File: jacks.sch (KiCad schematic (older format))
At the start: 72 parts, among them J1 PJ301CM, J10 PJ301BM, J11 PJ301BM, J12 PJ301BM, J13 PJ301BM, J14 PJ301BM, J15 PJ301BM, J16 PJ301BM, J17 PJ301BM, J18 PJ301BM, J19 PJ301BM, J2 PJ301CM, J20 PJ301BM, J21 PJ301BM, J22 PJ301BM, J23 PJ301BM, J24 PJ301BM, J25 PJ301BM, J26 PJ301BM, J3 PJ301BM, J4 PJ301BM, J5 PJ301BM, J6 PJ301BM, J7 PJ301BM, J8 PJ301BM, J9 PJ301BM, Q1 MMBT3904, Q2 MMBT3904, Q3 MMBT3904, Q4 MMBT3904, U1 VO0600T, U2 74LV1T34, U6 TL074

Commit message: added package field
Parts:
- C10, C11, C22, C23, C7, C8, R1, R12, R13, R14, R15, R16, R17, R18, R19, R2, R24, R25, R28, R29, R3, R30, R31, R35, R36, R37, R38, R4, R43, R44, R66, R76, R78, R79, R81, R82, R83, R84: Package (none) -> 0603
- D2: Package (none) -> SOD-123
- Q1, Q2, Q3, Q4: Package (none) -> SOT-23
- U1: Package (none) -> SOIC-8
- U2: Package (none) -> SOT-23-5
- U6: Package (none) -> SOIC-14
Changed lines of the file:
@@
 F 4 "ON Semiconductor" H 2100 1875 50  0001 C CNN "MFN"
 F 5 "MMBT3904LT1G" H 2100 1875 50  0001 C CNN "MFP"
+F 6 "SOT-23" H 2100 1875 50  0001 C CNN "Package"
 	1    1900 1700
 	1    0    0    -1
@@
 F 4 "Panasonic" H 1530 1800 50  0001 C CNN "MFN"
 F 5 "ERJ-3EKF1003V" H 1530 1800 50  0001 C CNN "MFP"
+F 6 "0603" H 1530 1800 50  0001 C CNN "Package"
 	1    1450 1700
 	0    1    1    0
@@
 F 4 "Panasonic" H 2080 1250 50  0001 C CNN "MFN"
 F 5 "ERJ-3EKF1002V" H 2080 1250 50  0001 C CNN "MFP"
+F 6 "0603" H 2080 1250 50  0001 C CNN "Package"
 	1    2000 1150
 	1    0    0    -1
@@
 F 4 "ON Semiconductor" H 2100 3475 50  0001 C CNN "MFN"
 F 5 "MMBT3904LT1G" H 2100 3475 50  0001 C CNN "MFP"
+F 6 "SOT-23" H 2100 3475 50  0001 C CNN "Package"
 	1    1900 3300
 	1    0    0    -1
@@
 F 4 "Panasonic" H 1530 3400 50  0001 C CNN "MFN"
 F 5 "ERJ-3EKF1003V" H 1530 3400 50  0001 C CNN "MFP"
+F 6 "0603" H 1530 3400 50  0001 C CNN "Package"
 	1    1450 3300
 	0    1    1    0
@@
 F 4 "Panasonic" H 2080 2850 50  0001 C CNN "MFN"
 F 5 "ERJ-3EKF1002V" H 2080 2850 50  0001 C CNN "MFP"
+F 6 "0603" H 2080 2850 50  0001 C CNN "Package"
 	1    2000 2750
 	1    0    0    -1
@@
 F 4 "ON Semiconductor" H 4100 1875 50  0001 C CNN "MFN"
 F 5 "MMBT3904LT1G" H 4100 1875 50  0001 C CNN "MFP"
+F 6 "SOT-23" H 4100 1875 50  0001 C CNN "Package"
 	1    3900 1700
 	1    0    0    -1
@@
 F 4 "Panasonic" H 4080 1250 50  0001 C CNN "MFN"
 F 5 "ERJ-3EKF1001V" H 4080 1250 50  0001 C CNN "MFP"
+F 6 "0603" H 4080 1250 50  0001 C CNN "Package"
 	1    4000 1150
 	1    0    0    -1
@@
 F 4 "Panasonic" H 3530 1800 50  0001 C CNN "MFN"
 F 5 "ERJ-3EKF1002V" H 3530 1800 50  0001 C CNN "MFP"
+F 6 "0603" H 3530 1800 50  0001 C CNN "Package"
 	1    3450 1700
 	0    1    1    0
@@
 F 4 "ON Semiconductor" H 4100 3575 50  0001 C CNN "MFN"
 F 5 "MMBT3904LT1G" H 4100 3575 50  0001 C CNN "MFP"
+F 6 "SOT-23" H 4100 3575 50  0001 C CNN "Package"
 	1    3900 3400
 	1    0    0    -1
@@
 F 4 "Panasonic" H 4080 2950 50  0001 C CNN "MFN"
 F 5 "ERJ-3EKF1001V" H 4080 2950 50  0001 C CNN "MFP"
+F 6 "0603" H 4080 2950 50  0001 C CNN "Package"
 	1    4000 2850
 	1    0    0    -1
@@
 F 4 "Panasonic" H 3530 3500 50  0001 C CNN "MFN"
 F 5 "ERJ-3EKF1002V" H 3530 3500 50  0001 C CNN "MFP"
+F 6 "0603" H 3530 3500 50  0001 C CNN "Package"
 	1    3450 3400
 	0    1    1    0
@@
 F 4 "Panasonic" H 10330 900 50  0001 C CNN "MFN"
 F 5 "ERJ-3EKF1001V" H 10330 900 50  0001 C CNN "MFP"
+F 6 "0603" H 10330 900 50  0001 C CNN "Package"
 	1    10250 800
 	0    1    1    0
@@
 F 4 "Panasonic" H 10330 1600 50  0001 C CNN "MFN"
 F 5 "ERJ-3EKF1001V" H 10330 1600 50  0001 C CNN "MFP"
+F 6 "0603" H 10330 1600 50  0001 C CNN "Package"
 	1    10250 1500
 	0    1    1    0
@@
 F 4 "Panasonic" H 10330 2300 50  0001 C CNN "MFN"
 F 5 "ERJ-3EKF1001V" H 10330 2300 50  0001 C CNN "MFP"
+F 6 "0603" H 10330 2300 50  0001 C CNN "Package"
 	1    10250 2200
 	0    1    1    0
@@
 F 4 "Panasonic" H 10330 3000 50  0001 C CNN "MFN"
 F 5 "ERJ-3EKF1001V" H 10330 3000 50  0001 C CNN "MFP"
+F 6 "0603" H 10330 3000 50  0001 C CNN "Package"
 	1    10250 2900
 	0    1    1    0
@@
 F 4 "Panasonic" H 10330 3700 50  0001 C CNN "MFN"
 F 5 "ERJ-3EKF1001V" H 10330 3700 50  0001 C CNN "MFP"
+F 6 "0603" H 10330 3700 50  0001 C CNN "Package"
 	1    10250 3600
 	0    1    1    0
@@
 F 4 "Panasonic" H 10330 4400 50  0001 C CNN "MFN"
 F 5 "ERJ-3EKF1001V" H 10330 4400 50  0001 C CNN "MFP"
+F 6 "0603" H 10330 4400 50  0001 C CNN "Package"
 	1    10250 4300
 	0    1    1    0
@@
 F 4 "Panasonic" H 10330 5100 50  0001 C CNN "MFN"
 F 5 "ERJ-3EKF1001V" H 10330 5100 50  0001 C CNN "MFP"
+F 6 "0603" H 10330 5100 50  0001 C CNN "Package"
 	1    10250 5000
 	0    1    1    0
@@
 F 4 "Panasonic" H 10330 5800 50  0001 C CNN "MFN"
 F 5 "ERJ-3EKF1001V" H 10330 5800 50  0001 C CNN "MFP"
+F 6 "0603" H 10330 5800 50  0001 C CNN "Package"
 	1    10250 5700
 	0    1    1    0
@@
 F 4 "Texas Instruments" H 2100 5500 50  0001 C CNN "MFN"
 F 5 "TL074CD" H 2100 5500 50  0001 C CNN "MFP"
+F 6 "SOIC-14" H 2100 5500 50  0001 C CNN "Package"
 	1    2100 5200
 	1    0    0    1
@@
 F 4 "Texas Instruments" H 2100 7000 50  0001 C CNN "MFN"
 F 5 "TL074CD" H 2100 7000 50  0001 C CNN "MFP"
+F 6 "SOIC-14" H 2100 7000 50  0001 C CNN "Package"
 	3    2100 6700
 	1    0    0    1
@@
 F 4 "Texas Instruments" H 4500 5500 50  0001 C CNN "MFN"
 F 5 "TL074CD" H 4500 5500 50  0001 C CNN "MFP"
+F 6 "SOIC-14" H 4500 5500 50  0001 C CNN "Package"
 	2    4500 5200
 	1    0    0    1
@@
 F 4 "Texas Instruments" H 4500 7000 50  0001 C CNN "MFN"
 F 5 "TL074CD" H 4500 7000 50  0001 C CNN "MFP"
+F 6 "SOIC-14" H 4500 7000 50  0001 C CNN "Package"
 	4    4500 6700
 	1    0    0    1
@@
 F 4 "Panasonic" H 1530 5200 50  0001 C CNN "MFN"
 F 5 "ERJ-3EKF1003V" H 1530 5200 50  0001 C CNN "MFP"
+F 6 "0603" H 1530 5200 50  0001 C CNN "Package"
 	1    1450 5100
 	0    1    1    0
@@
 F 4 "Panasonic" H 1530 4800 50  0001 C CNN "MFN"
 F 5 "ERJ-3EKF2003V" H 1530 4800 50  0001 C CNN "MFP"
+F 6 "0603" H 1530 4800 50  0001 C CNN "Package"
 	1    1450 4700
 	0    1    1    0
@@
 F 4 "Panasonic" H 2130 4700 50  0001 C CNN "MFN"
 F 5 "ERJ-3EKF3302V" H 2130 4700 50  0001 C CNN "MFP"
+F 6 "0603" H 2130 4700 50  0001 C CNN "Package"
 	1    2050 4600
 	0    1    1    0
@@
 F 4 "Murata" H 2075 4600 50  0001 C CNN "MFN"
 F 5 "GRM1885C1H102FA01J" H 2075 4600 50  0001 C CNN "MFP"
+F 6 "0603" H 2075 4600 50  0001 C CNN "Package"
 	1    2050 4400
 	0    1    1    0
@@
 F 4 "Panasonic" H 1530 6700 50  0001 C CNN "MFN"
 F 5 "ERJ-3EKF1003V" H 1530 6700 50  0001 C CNN "MFP"
+F 6 "0603" H 1530 6700 50  0001 C CNN "Package"
 	1    1450 6600
 	0    1    1    0
@@
 F 4 "Panasonic" H 1530 6300 50  0001 C CNN "MFN"
 F 5 "ERJ-3EKF2003V" H 1530 6300 50  0001 C CNN "MFP"
+F 6 "0603" H 1530 6300 50  0001 C CNN "Package"
 	1    1450 6200
 	0    1    1    0
@@
 F 4 "Panasonic" H 2130 6200 50  0001 C CNN "MFN"
 F 5 "ERJ-3EKF3302V" H 2130 6200 50  0001 C CNN "MFP"
+F 6 "0603" H 2130 6200 50  0001 C CNN "Package"
 	1    2050 6100
 	0    1    1    0
@@
 F 4 "Murata" H 2075 6100 50  0001 C CNN "MFN"
 F 5 "GRM1885C1H102FA01J" H 2075 6100 50  0001 C CNN "MFP"
+F 6 "0603" H 2075 6100 50  0001 C CNN "Package"
 	1    2050 5900
 	0    1    1    0
@@
 F 4 "Panasonic" H 3930 5200 50  0001 C CNN "MFN"
 F 5 "ERJ-3EKF1003V" H 3930 5200 50  0001 C CNN "MFP"
+F 6 "0603" H 3930 5200 50  0001 C CNN "Package"
 	1    3850 5100
 	0    1    1    0
@@
 F 4 "Panasonic" H 3930 4800 50  0001 C CNN "MFN"
 F 5 "ERJ-3EKF2003V" H 3930 4800 50  0001 C CNN "MFP"
+F 6 "0603" H 3930 4800 50  0001 C CNN "Package"
 	1    3850 4700
 	0    1    1    0
@@
 F 4 "Panasonic" H 4530 4700 50  0001 C CNN "MFN"
 F 5 "ERJ-3EKF3302V" H 4530 4700 50  0001 C CNN "MFP"
+F 6 "0603" H 4530 4700 50  0001 C CNN "Package"
 	1    4450 4600
 	0    1    1    0
@@
 F 4 "Murata" H 4475 4600 50  0001 C CNN "MFN"
 F 5 "GRM1885C1H102FA01J" H 4475 4600 50  0001 C CNN "MFP"
+F 6 "0603" H 4475 4600 50  0001 C CNN "Package"
 	1    4450 4400
 	0    1    1    0
@@
 F 4 "Panasonic" H 3930 6700 50  0001 C CNN "MFN"
 F 5 "ERJ-3EKF1003V" H 3930 6700 50  0001 C CNN "MFP"
+F 6 "0603" H 3930 6700 50  0001 C CNN "Package"
 	1    3850 6600
 	0    1    1    0
@@
 F 4 "Panasonic" H 3930 6300 50  0001 C CNN "MFN"
 F 5 "ERJ-3EKF2003V" H 3930 6300 50  0001 C CNN "MFP"
+F 6 "0603" H 3930 6300 50  0001 C CNN "Package"
 	1    3850 6200
 	0    1    1    0
@@
 F 4 "Panasonic" H 4530 6200 50  0001 C CNN "MFN"
 F 5 "ERJ-3EKF3302V" H 4530 6200 50  0001 C CNN "MFP"
+F 6 "0603" H 4530 6200 50  0001 C CNN "Package"
 	1    4450 6100
 	0    1    1    0
@@
 F 4 "Murata" H 4475 6100 50  0001 C CNN "MFN"
 F 5 "GRM1885C1H102FA01J" H 4475 6100 50  0001 C CNN "MFP"
+F 6 "0603" H 4475 6100 50  0001 C CNN "Package"
 	1    4450 5900
 	0    1    1    0
@@
 F 4 "Murata" H 5925 5700 50  0001 C CNN "MFN"
 F 5 "GRM188R71E104JA01J" H 5925 5700 50  0001 C CNN "MFP"
+F 6 "0603" H 5925 5700 50  0001 C CNN "Package"
 	1    5900 5500
 	1    0    0    -1
@@
 F 4 "Murata" H 5925 6200 50  0001 C CNN "MFN"
 F 5 "GRM188R71E104JA01J" H 5925 6200 50  0001 C CNN "MFP"
+F 6 "0603" H 5925 6200 50  0001 C CNN "Package"
 	1    5900 6000
 	1    0    0    -1
@@
 F 4 "Diodes Inc." H 6600 1950 50  0001 C CNN "MFN"
 F 5 "1N4148W-7-F" H 6600 1950 50  0001 C CNN "MFP"
+F 6 "SOD-123" H 6600 1950 50  0001 C CNN "Package"
 	1    6600 1750
 	0    1    1    0
@@
 F 4 "Panasonic" H 6430 1600 50  0001 C CNN "MFN"
 F 5 "ERJ-3EKF2200V" H 6430 1600 50  0001 C CNN "MFP"
+F 6 "0603" H 6430 1600 50  0001 C CNN "Package"
 	1    6350 1500
 	0    1    1    0
@@
 F 4 "Panasonic" H 7880 1550 50  0001 C CNN "MFN"
 F 5 "ERJ-3EKF1002V" H 7880 1550 50  0001 C CNN "MFP"
+F 6 "0603" H 7880 1550 50  0001 C CNN "Package"
 	1    7800 1450
 	1    0    0    -1
@@
 F 4 "Vishay" H 7250 1950 50  0001 C CNN "MFN"
 F 5 "VO0600T" H 7250 1950 50  0001 C CNN "MFP"
+F 6 "SOIC-8" H 7250 1950 50  0001 C CNN "Package"
 	1    7250 1600
 	1    0    0    -1
@@
 F 4 "Panasonic" H 7530 3400 50  0001 C CNN "MFN"
 F 5 "ERJ-3EKF2200V" H 7530 3400 50  0001 C CNN "MFP"
+F 6 "0603" H 7530 3400 50  0001 C CNN "Package"
 	1    7450 3300
 	0    -1   1    0
@@
 F 4 "Panasonic" H 7680 3050 50  0001 C CNN "MFN"
 F 5 "ERJ-3EKF2200V" H 7680 3050 50  0001 C CNN "MFP"
+F 6 "0603" H 7680 3050 50  0001 C CNN "Package"
 	1    7600 2950
 	-1   0    0    -1
@@
 F 4 "Texas Instruments" H 6600 2350 50  0001 C CNN "MFN"
 F 5 "SN74LV1T34DBVR" H 6600 2350 50  0001 C CNN "MFP"
+F 6 "SOT-23-5" H 6600 2350 50  0001 C CNN "Package"
 	1    6100 2600
 	1    0    0    -1

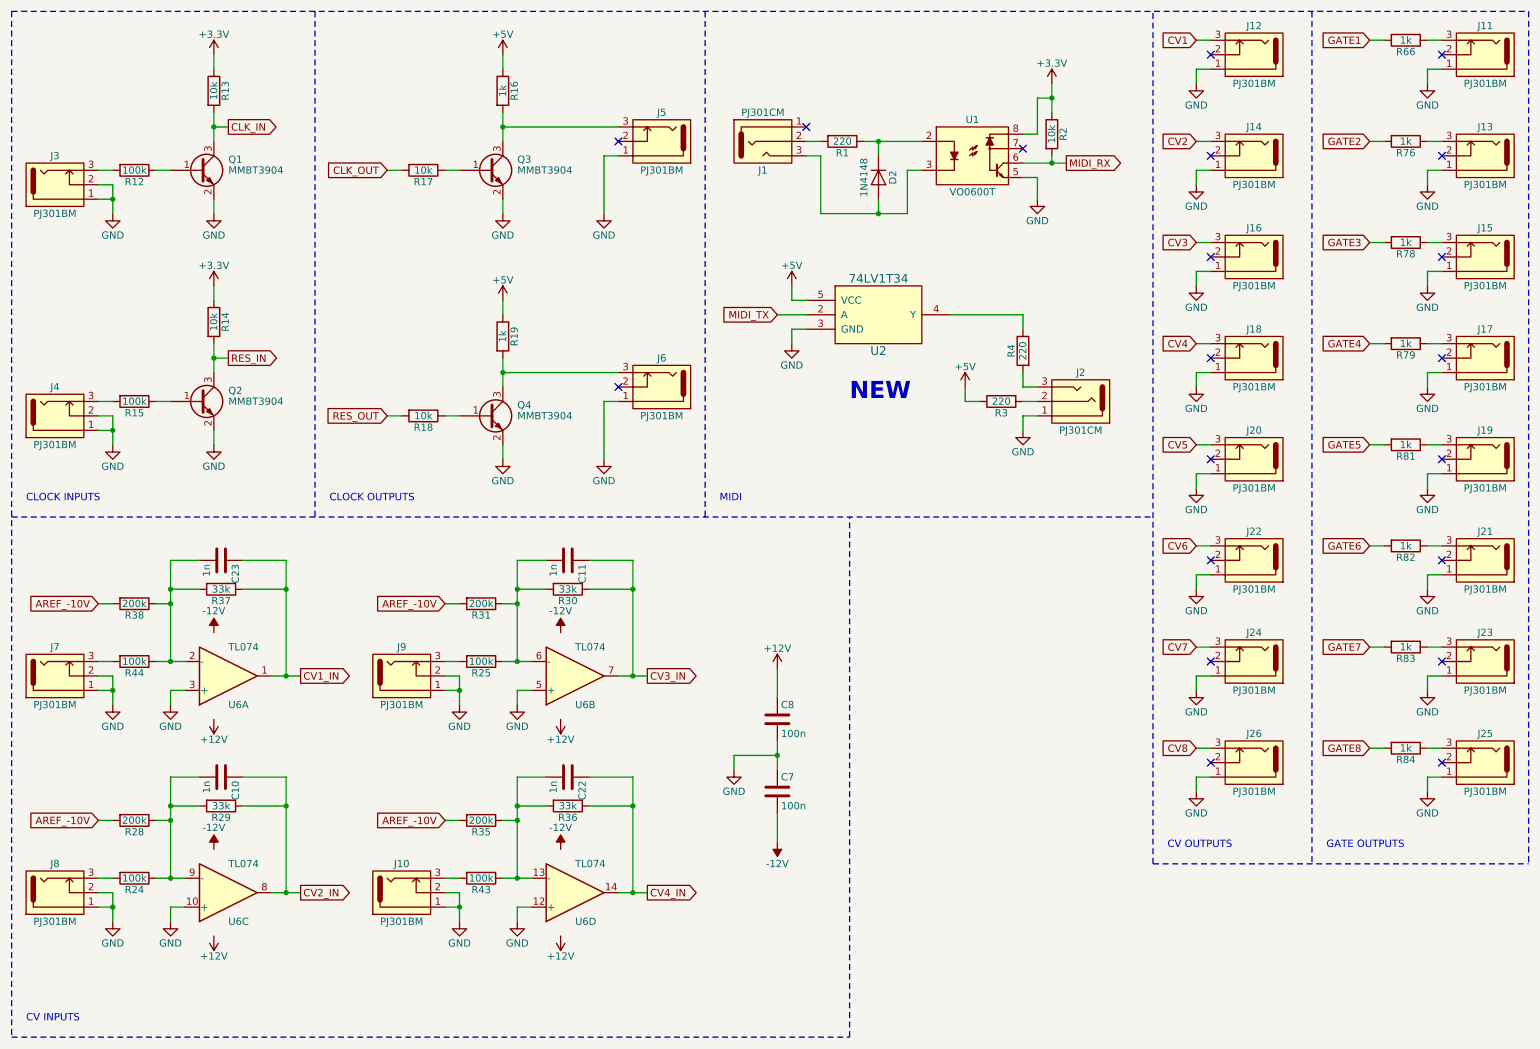
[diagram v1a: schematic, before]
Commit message: use rail-to-rail opamp for cv inputs
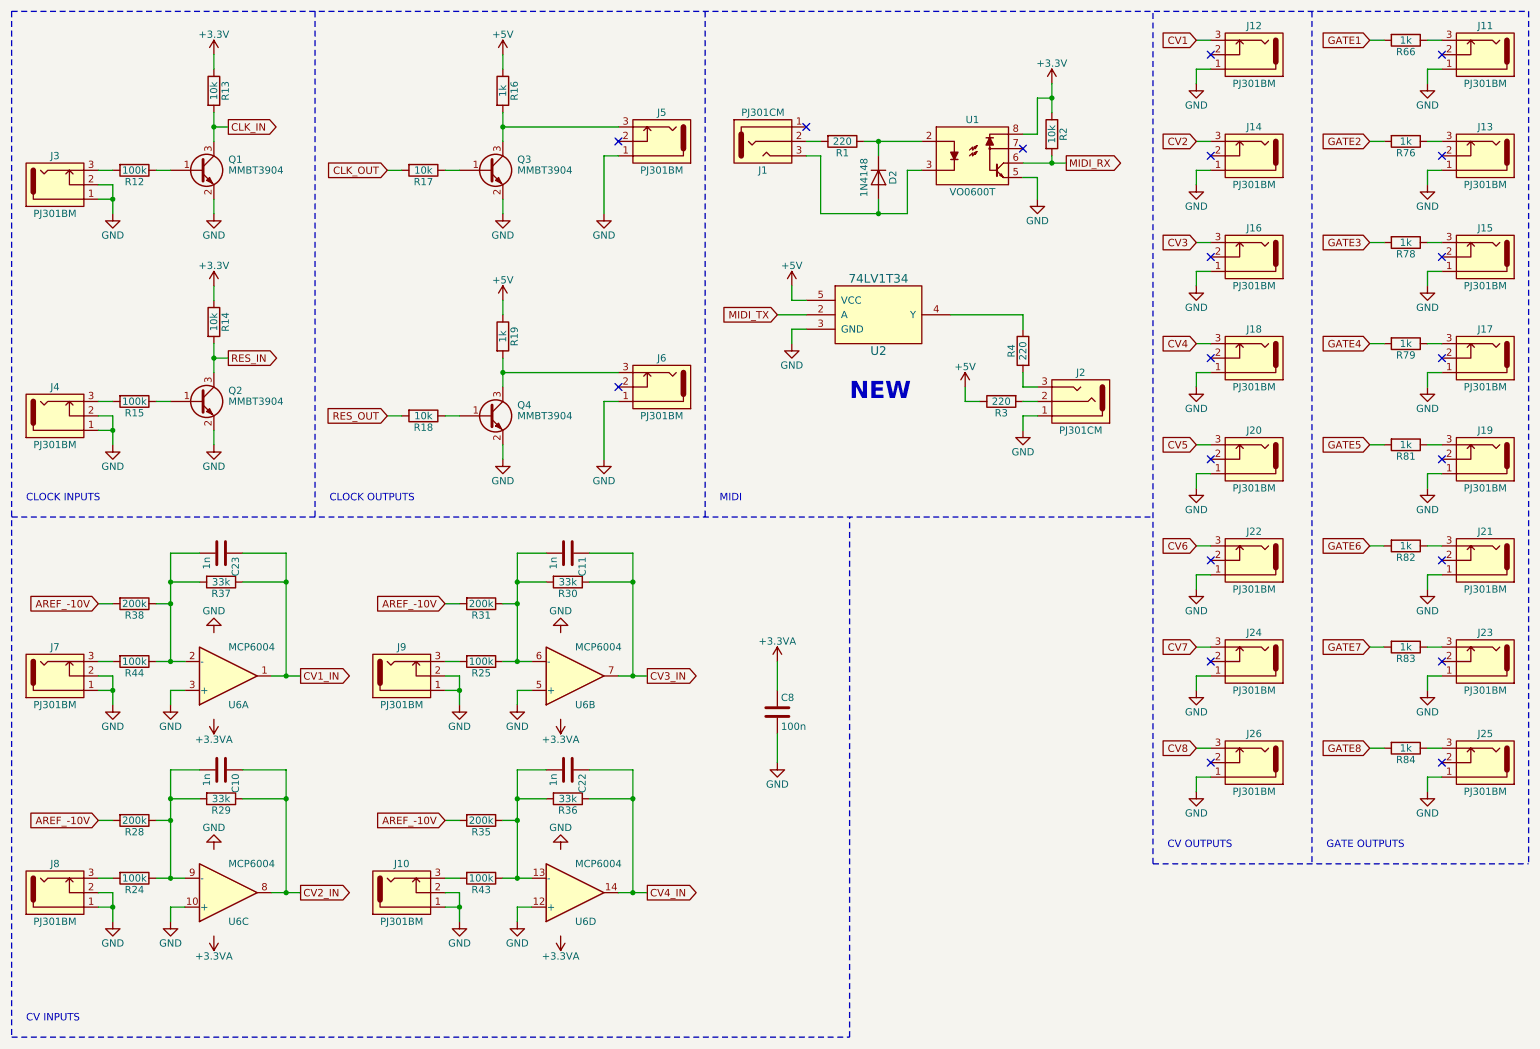
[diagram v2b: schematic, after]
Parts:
- removed C7: 100n, w_capacitor:C_0603, symbol C
- U6: value TL074 -> MCP6004; MFN Texas Instruments -> Microchip; MFP TL074CD -> MCP6004-I/SL
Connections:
- net +12V renamed +3.3VA
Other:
- moved on the sheet: C10, C11, C22, C23, C8, R29, R30, R36, R37

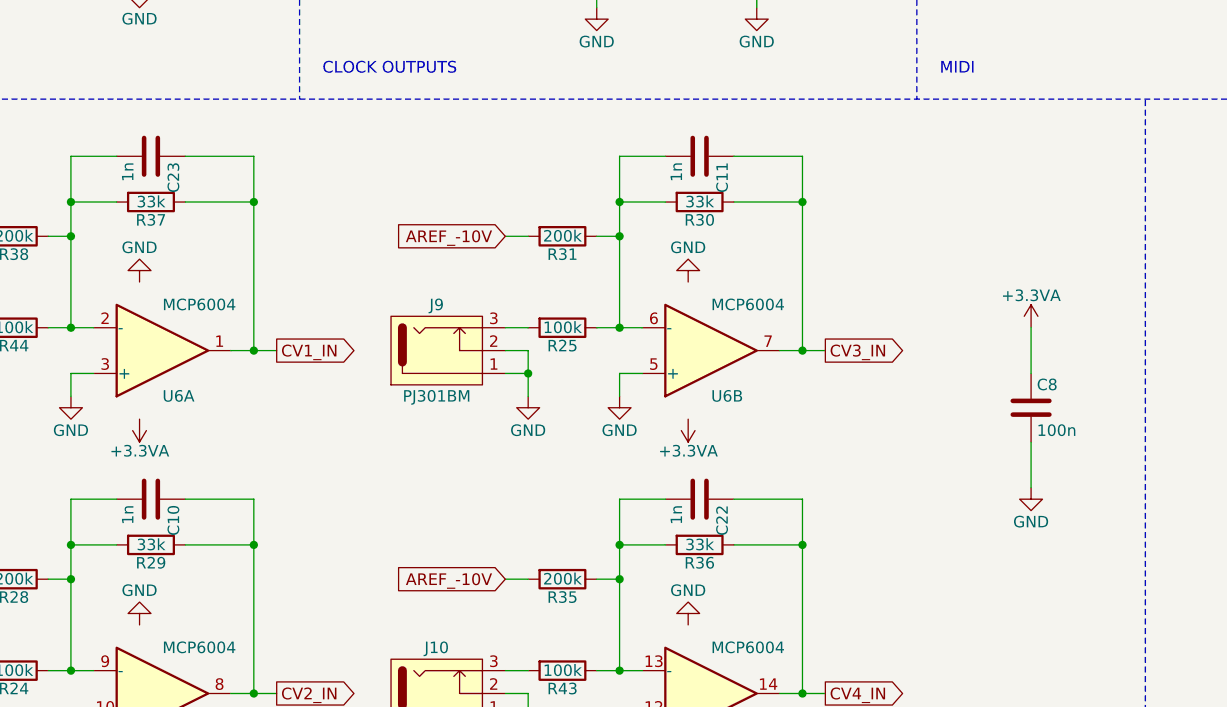
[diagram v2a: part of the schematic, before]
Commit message: renumbered components
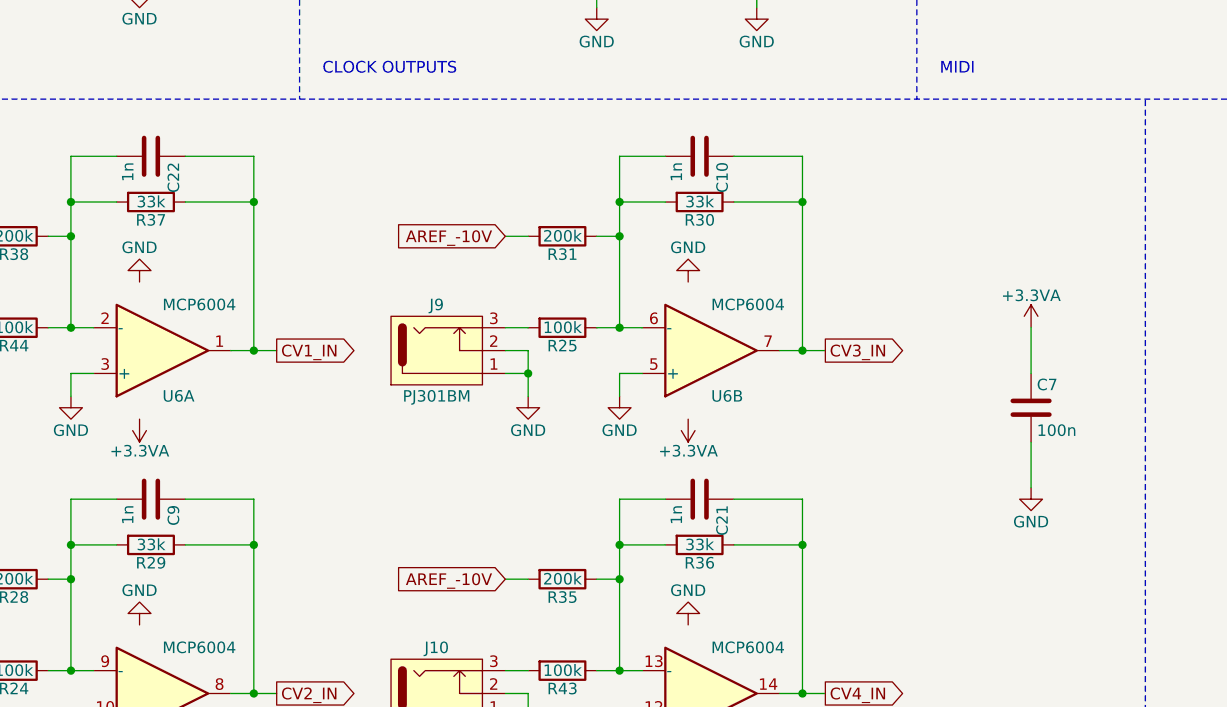
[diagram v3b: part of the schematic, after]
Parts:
- renumbered C11 to C10, C22 to C21, C23 to C22, C8 to C7, C10 to C9
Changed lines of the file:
@@
 $EndComp
 $Comp
-L C C23
+L C C22
 U 1 1 59DF7A26
 P 2050 4350
-F 0 "C23" H 2075 4450 50  0000 L CNN
+F 0 "C22" H 2075 4450 50  0000 L CNN
 F 1 "1n" H 2075 4250 50  0000 L CNN
 F 2 "w_capacitor:C_0603" H 2088 4200 50  0001 C CNN
@@
 $EndComp
 $Comp
-L C C10
+L C C9
 U 1 1 59DFAD47
 P 2050 5850
-F 0 "C10" H 2075 5950 50  0000 L CNN
+F 0 "C9" H 2075 5950 50  0000 L CNN
 F 1 "1n" H 2075 5750 50  0000 L CNN
 F 2 "w_capacitor:C_0603" H 2088 5700 50  0001 C CNN
@@
 $EndComp
 $Comp
-L C C11
+L C C10
 U 1 1 59DFB771
 P 4450 4350
-F 0 "C11" H 4475 4450 50  0000 L CNN
+F 0 "C10" H 4475 4450 50  0000 L CNN
 F 1 "1n" H 4475 4250 50  0000 L CNN
 F 2 "w_capacitor:C_0603" H 4488 4200 50  0001 C CNN
@@
 $EndComp
 $Comp
-L C C22
+L C C21
 U 1 1 59DFB7BE
 P 4450 5850
-F 0 "C22" H 4475 5950 50  0000 L CNN
+F 0 "C21" H 4475 5950 50  0000 L CNN
 F 1 "1n" H 4475 5750 50  0000 L CNN
 F 2 "w_capacitor:C_0603" H 4488 5700 50  0001 C CNN
@@
 $EndComp
 $Comp
-L C C8
+L C C7
 U 1 1 59E00FD6
 P 5900 5450
-F 0 "C8" H 5925 5550 50  0000 L CNN
+F 0 "C7" H 5925 5550 50  0000 L CNN
 F 1 "100n" H 5925 5350 50  0000 L CNN
 F 2 "w_capacitor:C_0603" H 5938 5300 50  0001 C CNN
